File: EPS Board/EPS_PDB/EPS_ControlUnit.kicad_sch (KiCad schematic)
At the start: 35 parts, among them Q1 PMOS, Q2 PMOS, SW1 SW_SPDT, U19 SN65HVD256D, U3 SN65HVD256D, U4 STM32L476VET6, U5 TPS3824-33QDBVRQ1, Y1 32MHz

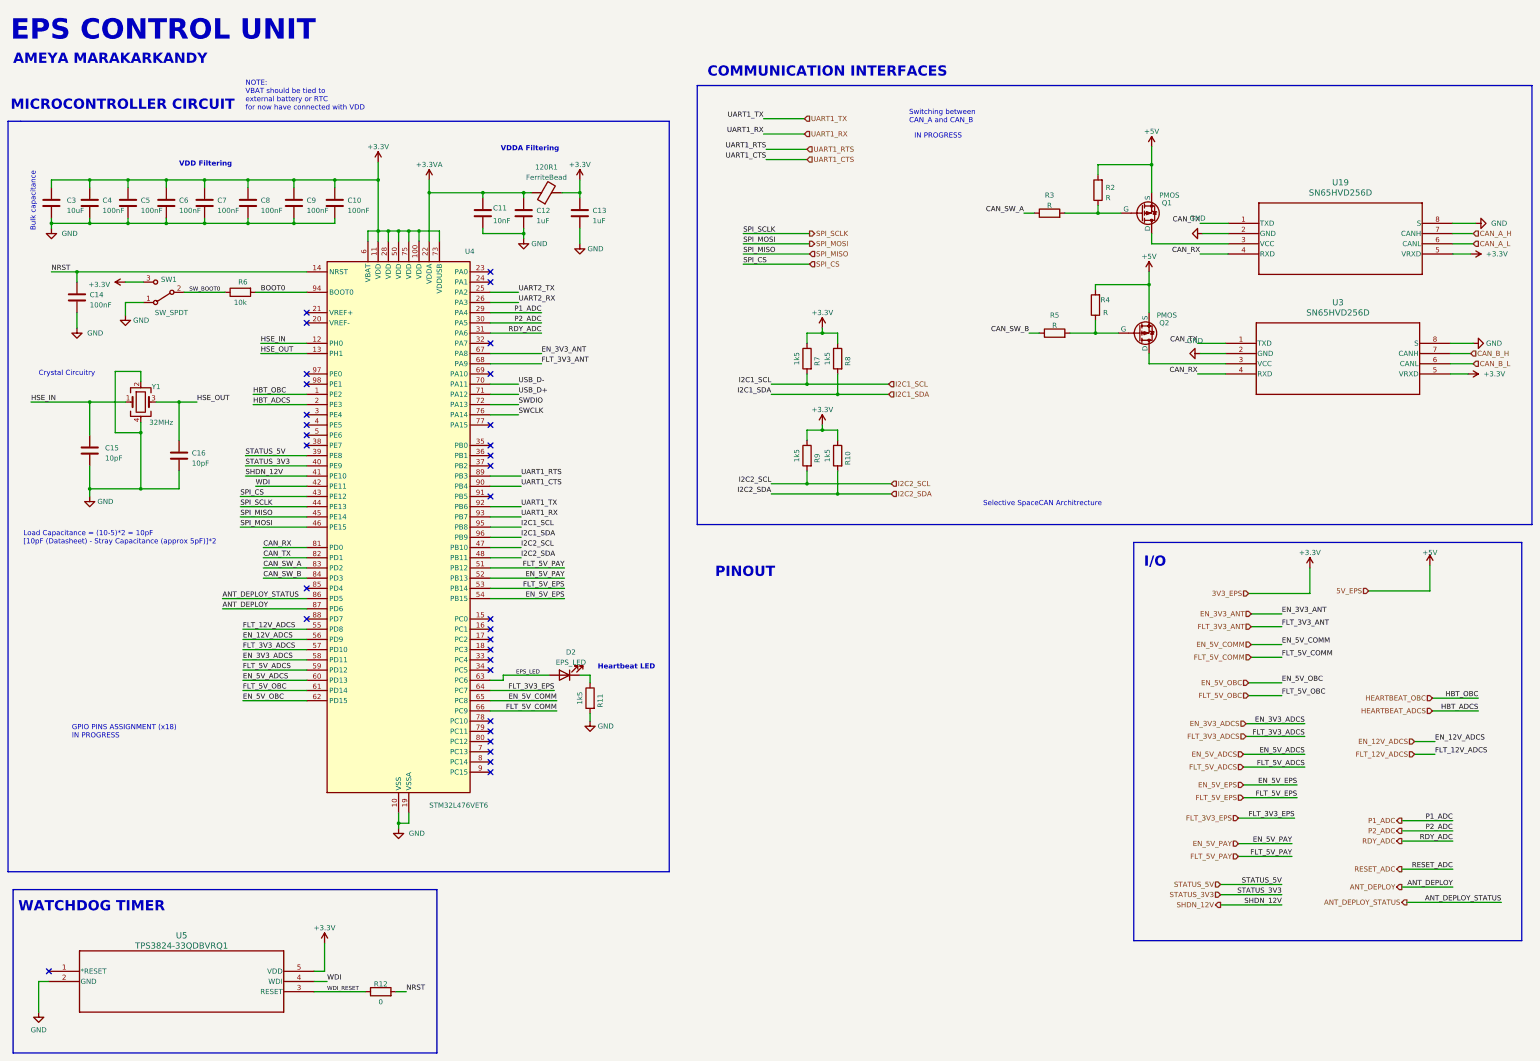
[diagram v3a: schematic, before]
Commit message: Reference voltage ic, clock, ADC schematic done
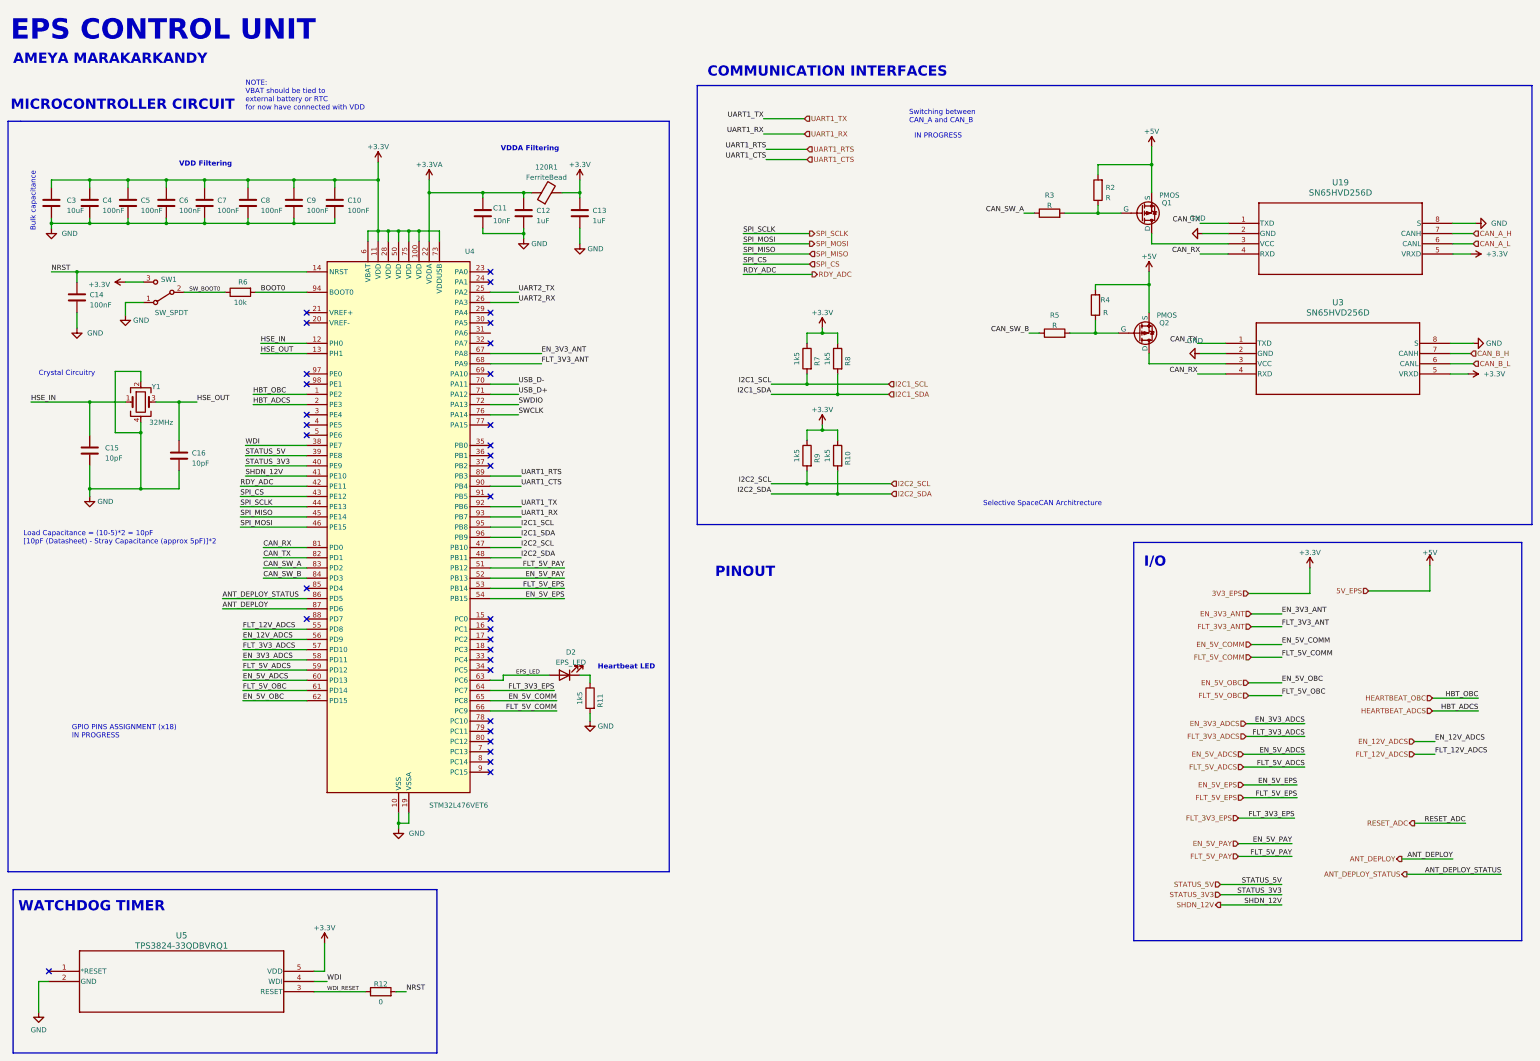
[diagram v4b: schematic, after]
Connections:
- net RDY_ADC: now also U4.42 (PE11); no longer U4.31 (PA6)
- net WDI: now also U4.38 (PE7); no longer U4.42 (PE11)
- net P1_ADC: no longer names the net of U4.29 (PA4)
- net P2_ADC: no longer names the net of U4.30 (PA5)
- no-connect marks 32 -> 33
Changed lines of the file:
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@@
 	)
 	(no_connect
+		(at 140.97 93.345)
+	)
+	(no_connect
 		(at 140.97 202.565)
 	)
@@
 	)
 	(no_connect
+		(at 140.97 95.885)
+	)
+	(no_connect
 		(at 95.25 121.285)
 	)
@@
 	)
 	(no_connect
-		(at 95.25 126.365)
-	)
-	(no_connect
 		(at 140.97 177.165)
 	)
@@
 	(wire
 		(pts
-			(xy 367.665 219.71) (xy 380.365 219.71)
-		)
-		(stroke
-			(width 0)
-			(type default)
-		)
-	)
-	(wire
-		(pts
 			(xy 97.155 259.715) (xy 100.33 259.715)
 		)
@@
 	(wire
 		(pts
-			(xy 367.665 231.775) (xy 380.365 231.775)
+			(xy 370.84 220.345) (xy 383.54 220.345)
 		)
 		(stroke
@@
 	(wire
 		(pts
-			(xy 367.665 236.22) (xy 380.365 236.22)
+			(xy 367.665 229.235) (xy 380.365 229.235)
 		)
 		(stroke
@@
 	(wire
 		(pts
-			(xy 367.665 224.79) (xy 380.365 224.79)
+			(xy 80.01 126.365) (xy 95.25 126.365)
 		)
 		(stroke
@@
 	(wire
 		(pts
-			(xy 140.97 98.425) (xy 153.67 98.425)
-		)
-		(stroke
-			(width 0)
-			(type default)
-		)
-	)
-	(wire
-		(pts
 			(xy 210.82 111.125) (xy 219.71 111.125)
 		)
@@
 	(wire
 		(pts
-			(xy 140.97 95.885) (xy 153.67 95.885)
-		)
-		(stroke
-			(width 0)
-			(type default)
-		)
-	)
-	(wire
-		(pts
 			(xy 95.25 177.165) (xy 79.375 177.165)
 		)
@@
 	(wire
 		(pts
-			(xy 140.97 93.345) (xy 153.67 93.345)
-		)
-		(stroke
-			(width 0)
-			(type default)
-		)
-	)
-	(wire
-		(pts
 			(xy 84.455 154.305) (xy 95.25 154.305)
 		)
@@
 	(wire
 		(pts
+			(xy 95.25 136.525) (xy 78.74 136.525)
+		)
+		(stroke
+			(width 0)
+			(type default)
+		)
+	)
+	(wire
+		(pts
 			(xy 328.93 195.58) (xy 343.535 195.58)
 		)
@@
 	(wire
 		(pts
-			(xy 322.58 235.585) (xy 337.82 235.585)
+			(xy 220.98 83.82) (xy 203.835 83.82)
 		)
 		(stroke
@@
 	(wire
 		(pts
-			(xy 60.325 69.85) (xy 60.325 71.12)
+			(xy 322.58 235.585) (xy 337.82 235.585)
 		)
 		(stroke
@@
 	(wire
 		(pts
-			(xy 92.075 60.325) (xy 92.075 62.23)
+			(xy 60.325 69.85) (xy 60.325 71.12)
 		)
 		(stroke
@@
 	(wire
 		(pts
-			(xy 95.25 172.085) (xy 79.375 172.085)
+			(xy 92.075 60.325) (xy 92.075 62.23)
 		)
 		(stroke
@@
 	(wire
 		(pts
-			(xy 220.345 73.66) (xy 203.835 73.66)
+			(xy 95.25 172.085) (xy 79.375 172.085)
 		)
 		(stroke
@@
 	(wire
 		(pts
-			(xy 367.665 222.25) (xy 380.365 222.25)
+			(xy 220.345 73.66) (xy 203.835 73.66)
 		)
 		(stroke
@@
 	(wire
 		(pts
-			(xy 82.55 136.525) (xy 95.25 136.525)
-		)
-		(stroke
-			(width 0)
-			(type default)
-		)
-	)
-	(wire
-		(pts
 			(xy 50.165 90.805) (xy 50.165 93.98)
 		)
@@
 	(wire
 		(pts
-			(xy 368.935 240.03) (xy 392.43 240.03)
+			(xy 368.935 233.045) (xy 392.43 233.045)
 		)
 		(stroke
@@
 		)
 	)
-	(label "P1_ADC"
-		(at 153.67 93.345 180)
-		(fields_autoplaced yes)
-		(effects
-			(font
-				(size 1.27 1.27)
-			)
-			(justify right bottom)
-		)
-	)
 	(label "EN_5V_OBC"
 		(at 79.375 189.865 0)
@@
 		)
 	)
-	(label "P2_ADC"
-		(at 153.67 95.885 180)
-		(fields_autoplaced yes)
-		(effects
-			(font
-				(size 1.27 1.27)
-			)
-			(justify right bottom)
-		)
-	)
 	(label "FLT_3V3_EPS"
 		(at 340.995 219.075 180)
@@
 		)
 	)
-	(label "RDY_ADC"
-		(at 380.365 224.79 180)
-		(fields_autoplaced yes)
-		(effects
-			(font
-				(size 1.27 1.27)
-			)
-			(justify right bottom)
-		)
-	)
 	(label "SPI_SCLK"
 		(at 203.835 73.66 0)
@@
 	)
 	(label "RESET_ADC"
-		(at 380.365 231.775 180)
+		(at 383.54 220.345 180)
 		(fields_autoplaced yes)
 		(effects
@@
 		)
 	)
+	(label "WDI"
+		(at 80.01 126.365 0)
+		(fields_autoplaced yes)
+		(effects
+			(font
+				(size 1.27 1.27)
+			)
+			(justify left bottom)
+		)
+	)
 	(label "USB_D-"
 		(at 147.955 111.125 0)
@@
 		)
 	)
+	(label "RDY_ADC"
+		(at 78.74 136.525 0)
+		(fields_autoplaced yes)
+		(effects
+			(font
+				(size 1.27 1.27)
+			)
+			(justify left bottom)
+		)
+	)
 	(label "STATUS_5V"
 		(at 80.01 128.905 0)
@@
 	)
 	(label "ANT_DEPLOY_STATUS"
-		(at 392.43 240.03 180)
+		(at 392.43 233.045 180)
 		(fields_autoplaced yes)
 		(effects
@@
 		)
 	)
-	(label "P1_ADC"
-		(at 380.365 219.71 180)
+	(label "RDY_ADC"
+		(at 203.835 83.82 0)
 		(fields_autoplaced yes)
 		(effects
@@
 				(size 1.27 1.27)
 			)
-			(justify right bottom)
+			(justify left bottom)
 		)
 	)
@@
 	)
 	(label "ANT_DEPLOY"
-		(at 380.365 236.22 180)
+		(at 380.365 229.235 180)
 		(fields_autoplaced yes)
 		(effects
@@
 		)
 	)
-	(label "WDI"
-		(at 82.55 136.525 0)
-		(fields_autoplaced yes)
-		(effects
-			(font
-				(size 1.27 1.27)
-			)
-			(justify left bottom)
-		)
-	)
 	(label "SPI_SCLK"
 		(at 78.74 141.605 0)
@@
 		)
 	)
-	(label "P2_ADC"
-		(at 380.365 222.25 180)
-		(fields_autoplaced yes)
-		(effects
-			(font
-				(size 1.27 1.27)
-			)
-			(justify right bottom)
-		)
-	)
 	(label "EN_3V3_ANT"
 		(at 153.67 103.505 0)
@@
 		)
 	)
-	(label "RDY_ADC"
-		(at 153.67 98.425 180)
-		(fields_autoplaced yes)
-		(effects
-			(font
-				(size 1.27 1.27)
-			)
-			(justify right bottom)
-		)
-	)
 	(label "HSE_IN"
 		(at 83.82 100.965 0)
@@
 		)
 	)
+	(hierarchical_label "RDY_ADC"
+		(shape output)
+		(at 220.98 83.82 0)
+		(fields_autoplaced yes)
+		(effects
+			(font
+				(size 1.27 1.27)
+			)
+			(justify left)
+		)
+	)
 	(hierarchical_label "STATUS_5V"
 		(shape input)
@@
 	(hierarchical_label "RESET_ADC"
 		(shape output)
-		(at 367.665 231.775 180)
+		(at 370.84 220.345 180)
 		(fields_autoplaced yes)
 		(effects
@@
 		)
 	)
-	(hierarchical_label "RDY_ADC"
-		(shape output)
-		(at 367.665 224.79 180)
-		(fields_autoplaced yes)
-		(effects
-			(font
-				(size 1.27 1.27)
-			)
-			(justify right)
-		)
-	)
 	(hierarchical_label "I2C1_SCL"
 		(shape input)
@@
 	(hierarchical_label "ANT_DEPLOY_STATUS"
 		(shape output)
-		(at 368.935 240.03 180)
-		(fields_autoplaced yes)
-		(effects
-			(font
-				(size 1.27 1.27)
-			)
-			(justify right)
-		)
-	)
-	(hierarchical_label "P2_ADC"
-		(shape output)
-		(at 367.665 222.25 180)
+		(at 368.935 233.045 180)
 		(fields_autoplaced yes)
 		(effects
@@
 	(hierarchical_label "ANT_DEPLOY"
 		(shape output)
-		(at 367.665 236.22 180)
+		(at 367.665 229.235 180)
 		(fields_autoplaced yes)
 		(effects
@@
 		(fields_autoplaced yes)
 		(effects
-			(font
-				(size 1.27 1.27)
-			)
-			(justify right)
-		)
-	)
-	(hierarchical_label "P1_ADC"
-		(shape output)
-		(at 367.665 219.71 180)
-		(fields_autoplaced yes)
-		(effects

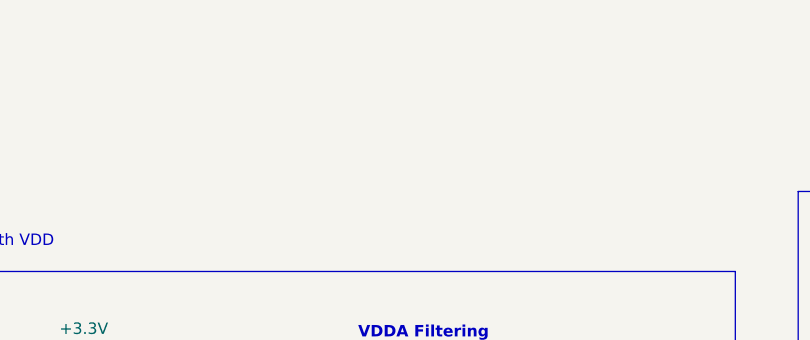
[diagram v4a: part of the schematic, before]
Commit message: texts added in schematics for clarity
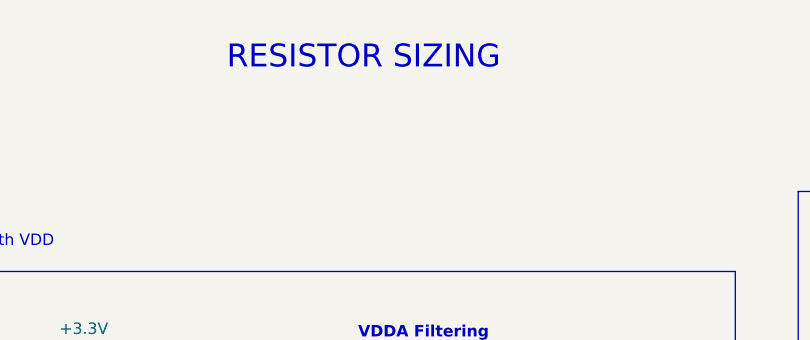
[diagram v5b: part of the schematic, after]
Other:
- note added: "RESISTOR SIZING"
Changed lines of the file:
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@@
+		)
+	)
+	(text "RESISTOR SIZING"
+		(exclude_from_sim no)
+		(at 128.905 23.495 0)
+		(effects
+			(font
+				(size 2.54 2.54)
+			)
+			(justify left bottom)
 		)
 	)

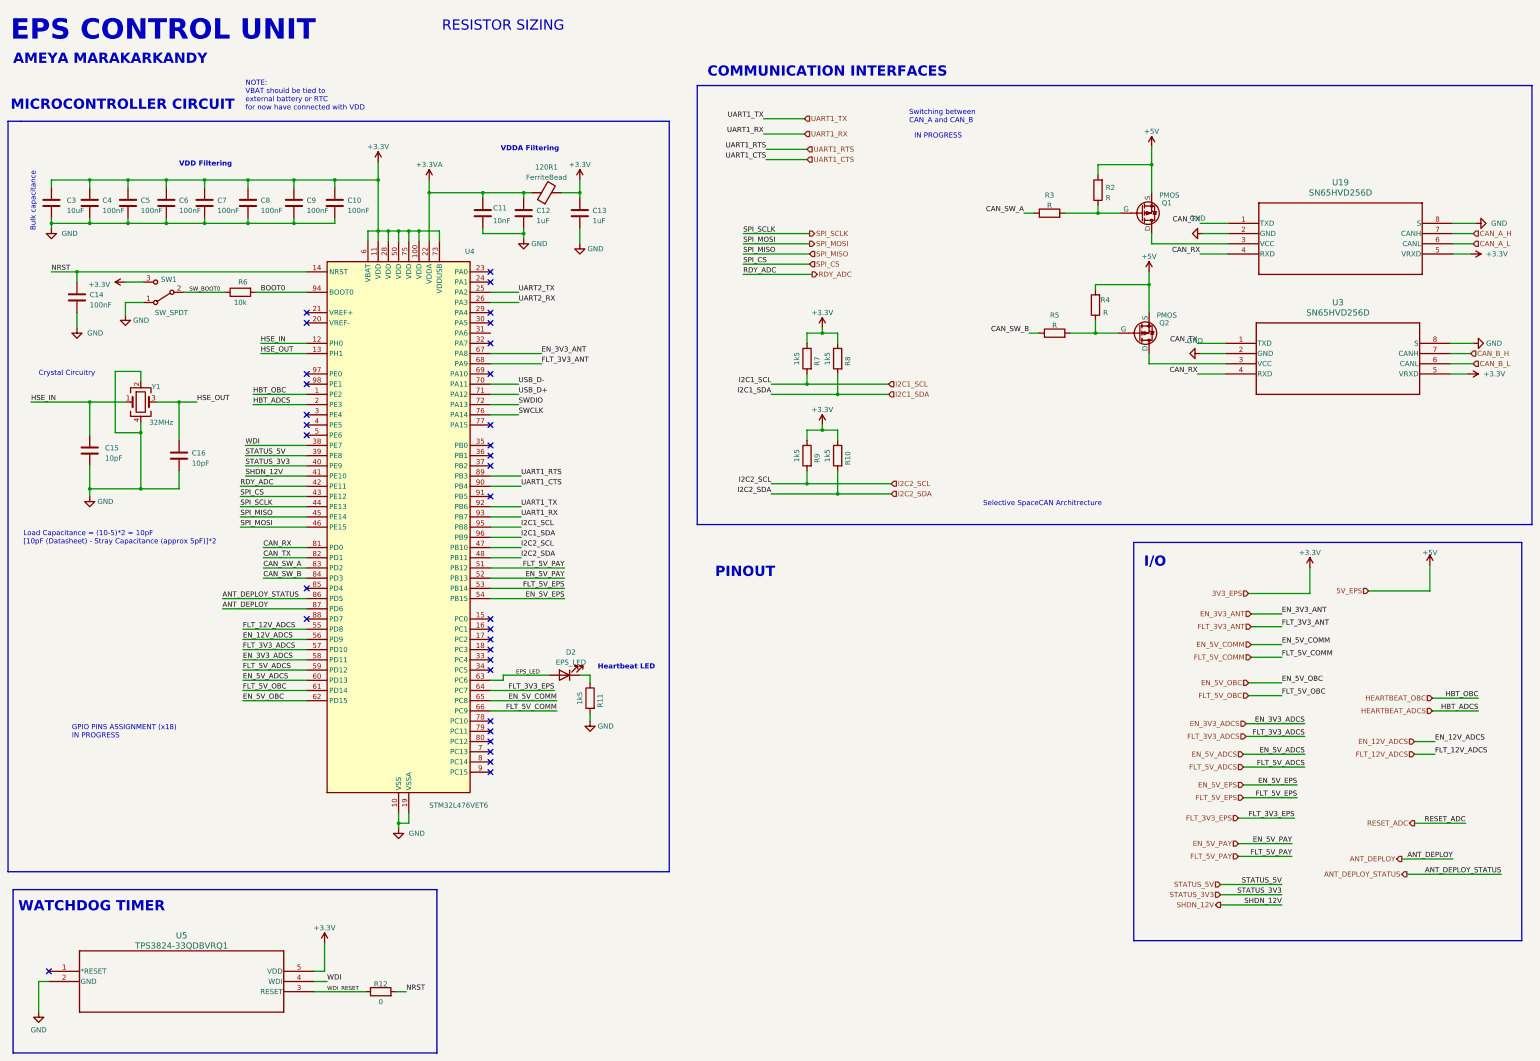
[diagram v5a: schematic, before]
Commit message: Footprint assignment on EPS PDB Board
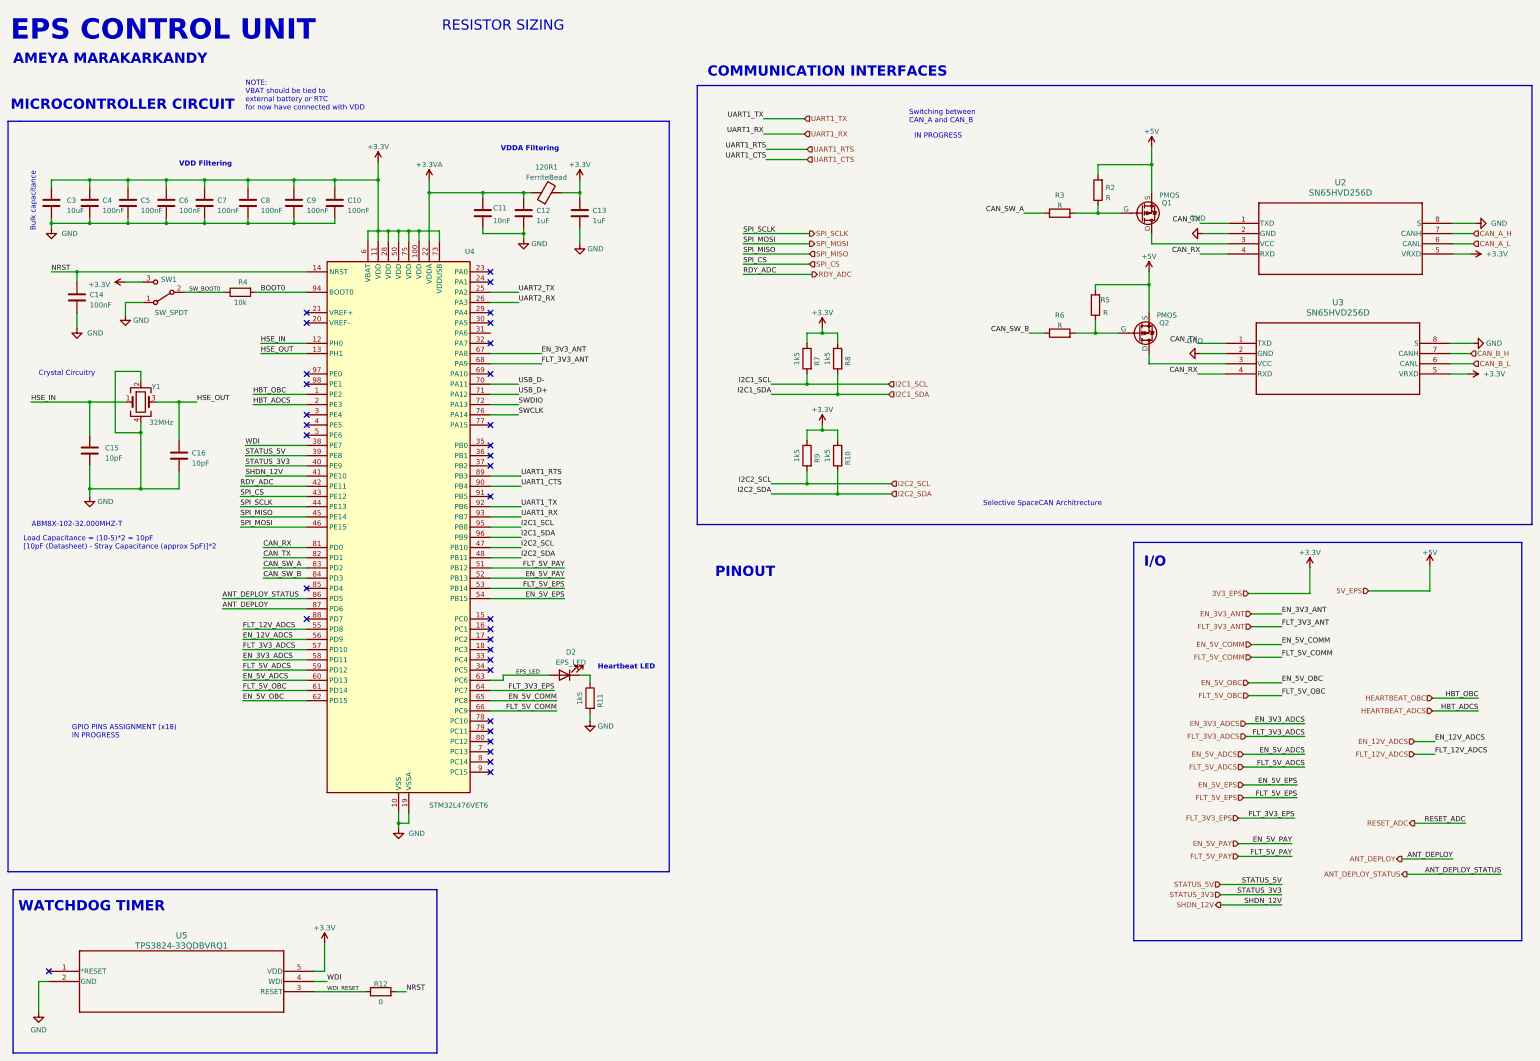
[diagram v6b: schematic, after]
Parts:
- 120R1, R10, R11, R12, R2, R3, R7, R8, R9: footprint (none) -> Resistor_SMD:R_0805_2012Metric
- C10, C11, C12, C13, C14, C15, C16, C3, C4, C5, C6, C7, C8, C9: footprint (none) -> Capacitor_SMD:C_0805_2012Metric
- D2: footprint (none) -> LED_SMD:LED_0805_2012Metric
- Q1, Q2: footprint (none) -> Package_TO_SOT_SMD:SOT-23-3
- R4: renamed from R6; footprint (none) -> Resistor_SMD:R_0805_2012Metric
- R5: renamed from R4; footprint (none) -> Resistor_SMD:R_0805_2012Metric
- R6: renamed from R5; footprint (none) -> Resistor_SMD:R_0805_2012Metric
- SW1: footprint (none) -> Button_Switch_SMD:SW_SPST_B3S-1100
- U2: renamed from U19; footprint D8 -> SN65HVD256D:D8
- U3: footprint D8 -> SN65HVD256D:D8
- U4: footprint (none) -> Package_QFP:LQFP-100_14x14mm_P0.5mm
- U5: footprint (none) -> TPS3824:tps3824
- Y1: footprint (none) -> Crystal:Crystal_SMD_Abracon_ABM8AIG-4Pin_3.2x2.5mm
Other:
- note added: "ABM8X-102-32.000MHZ-T"
- moved on the sheet: R3, R6
